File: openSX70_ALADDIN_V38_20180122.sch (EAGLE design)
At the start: 47 parts, among them Q1 5.8A/30V/35mΩ, Q2 5.8A/30V/35mΩ, U1 ATMEGA328P_TQFP, U3 BH1750FVI-TR, Y1 CSTCE16M0V53-R0

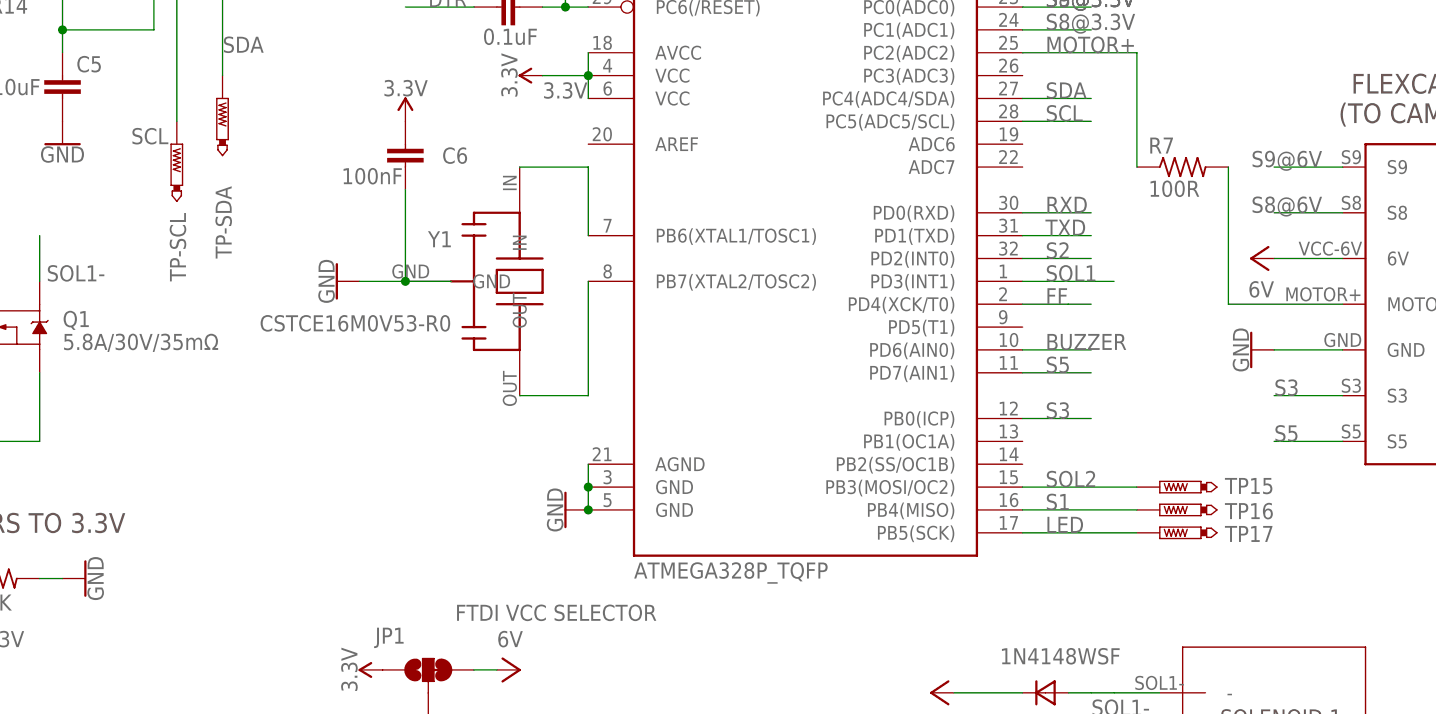
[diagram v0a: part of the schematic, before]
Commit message: "Saved" Aladdin regarding light-seal issue. Will manufacture. Current 2.8
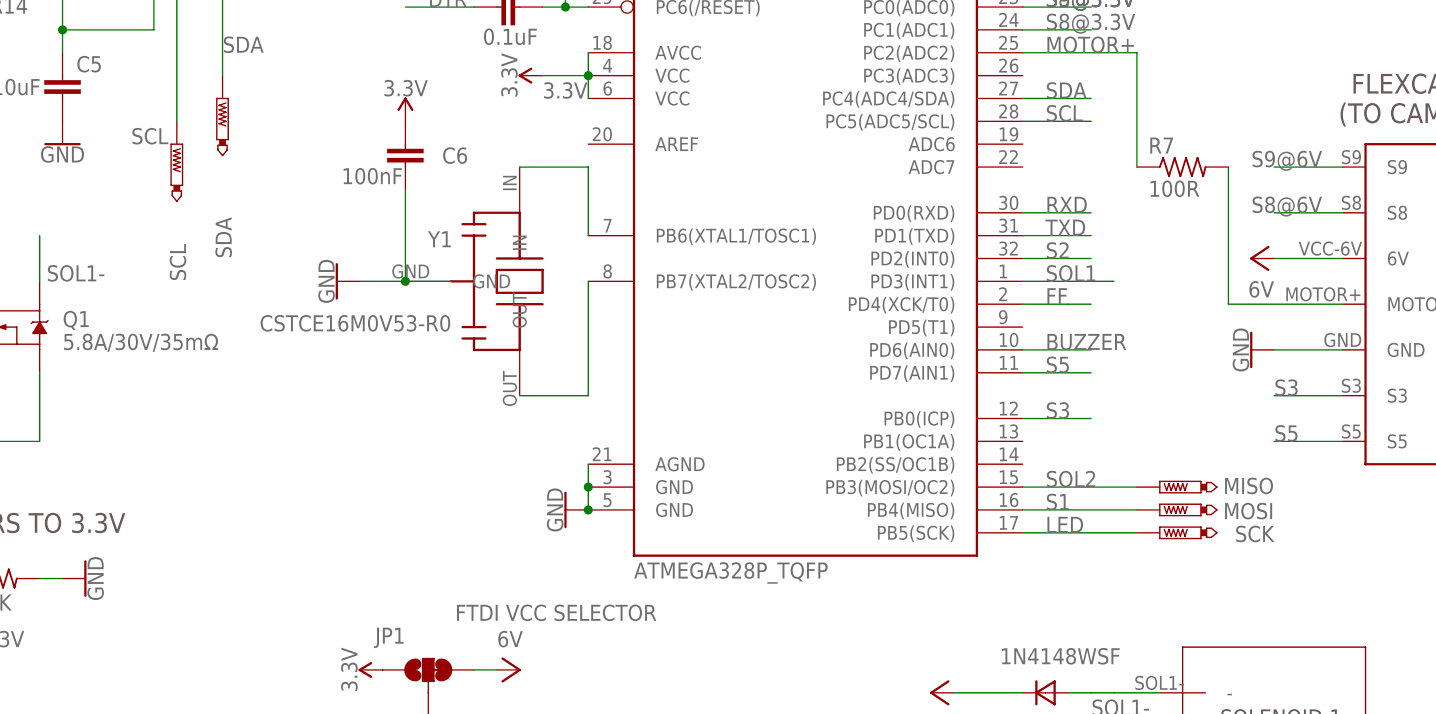
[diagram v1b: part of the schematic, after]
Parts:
- renumbered TP-SCL to SCL, TP-SDA to SDA, TP15 to MISO, TP16 to MOSI, TP17 to SCK
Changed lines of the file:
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@@
 <part name="P+9" library="openSX70" deviceset="VCC" device="" value="6V"/>
 <part name="GND4" library="SparkFun-PowerSymbols" library_urn="urn:adsk.eagle:library:530" deviceset="GND" device=""/>
-<part name="TP15" library="testpad" library_urn="urn:adsk.eagle:library:385" deviceset="PTR1" device="TP08R" package3d_urn="urn:adsk.eagle:package:27956/1" value="PTR1TP08R"/>
-<part name="TP16" library="testpad" library_urn="urn:adsk.eagle:library:385" deviceset="PTR1" device="TP08R" package3d_urn="urn:adsk.eagle:package:27956/1" value="PTR1TP08R"/>
-<part name="TP17" library="testpad" library_urn="urn:adsk.eagle:library:385" deviceset="PTR1" device="TP08R" package3d_urn="urn:adsk.eagle:package:27956/1" value="PTR1TP08R"/>
-<part name="TP-SDA" library="testpad" library_urn="urn:adsk.eagle:library:385" deviceset="PTR1" device="TP08R" package3d_urn="urn:adsk.eagle:package:27956/1" value="PTR1TP08R"/>
-<part name="TP-SCL" library="testpad" library_urn="urn:adsk.eagle:library:385" deviceset="PTR1" device="TP08R" package3d_urn="urn:adsk.eagle:package:27956/1" value="PTR1TP08R"/>
+<part name="MISO" library="testpad" library_urn="urn:adsk.eagle:library:385" deviceset="PTR1" device="TP08R" package3d_urn="urn:adsk.eagle:package:27956/1" value="PTR1TP08R"/>
+<part name="MOSI" library="testpad" library_urn="urn:adsk.eagle:library:385" deviceset="PTR1" device="TP08R" package3d_urn="urn:adsk.eagle:package:27956/1" value="PTR1TP08R"/>
+<part name="SCK" library="testpad" library_urn="urn:adsk.eagle:library:385" deviceset="PTR1" device="TP08R" package3d_urn="urn:adsk.eagle:package:27956/1" value="PTR1TP08R"/>
+<part name="SDA" library="testpad" library_urn="urn:adsk.eagle:library:385" deviceset="PTR1" device="TP08R" package3d_urn="urn:adsk.eagle:package:27956/1" value="PTR1TP08R"/>
+<part name="SCL" library="testpad" library_urn="urn:adsk.eagle:library:385" deviceset="PTR1" device="TP08R" package3d_urn="urn:adsk.eagle:package:27956/1" value="PTR1TP08R"/>
 </parts>
 <sheets>
@@
 <attribute name="VALUE" x="70.866" y="45.72" size="1.778" layer="96" rot="R270" align="top-center"/>
 </instance>
-<instance part="TP15" gate="G$1" x="208.28" y="73.66" smashed="yes" rot="R90">
+<instance part="MISO" gate="G$1" x="208.28" y="73.66" smashed="yes" rot="R90">
 <attribute name="NAME" x="220.98" y="74.676" size="1.778" layer="95" rot="R180"/>
 <attribute name="TP_SIGNAL_NAME" x="210.82" y="74.93" size="1.778" layer="97" rot="R90"/>
 </instance>
-<instance part="TP16" gate="G$1" x="208.28" y="71.12" smashed="yes" rot="R90">
+<instance part="MOSI" gate="G$1" x="208.28" y="71.12" smashed="yes" rot="R90">
 <attribute name="NAME" x="220.98" y="71.882" size="1.778" layer="95" rot="R180"/>
 <attribute name="TP_SIGNAL_NAME" x="210.82" y="72.39" size="1.778" layer="97" rot="R90"/>
 </instance>
-<instance part="TP17" gate="G$1" x="208.28" y="68.58" smashed="yes" rot="R90">
+<instance part="SCK" gate="G$1" x="208.28" y="68.58" smashed="yes" rot="R90">
 <attribute name="NAME" x="220.98" y="69.342" size="1.778" layer="95" rot="R180"/>
 <attribute name="TP_SIGNAL_NAME" x="210.82" y="69.85" size="1.778" layer="97" rot="R90"/>
 </instance>
-<instance part="TP-SDA" gate="G$1" x="104.14" y="116.84" smashed="yes">
+<instance part="SDA" gate="G$1" x="104.14" y="116.84" smashed="yes">
 <attribute name="NAME" x="105.156" y="99.06" size="1.778" layer="95" rot="R90"/>
 <attribute name="TP_SIGNAL_NAME" x="105.41" y="114.3" size="1.778" layer="97"/>
 </instance>
-<instance part="TP-SCL" gate="G$1" x="99.06" y="111.76" smashed="yes">
+<instance part="SCL" gate="G$1" x="99.06" y="111.76" smashed="yes">
 <attribute name="NAME" x="100.076" y="96.52" size="1.778" layer="95" rot="R90"/>
 <attribute name="TP_SIGNAL_NAME" x="100.33" y="109.22" size="1.778" layer="97"/>
@@
 <wire x1="193.04" y1="71.12" x2="205.74" y2="71.12" width="0.1524" layer="91"/>
 <label x="195.58" y="71.12" size="1.778" layer="95"/>
-<pinref part="TP16" gate="G$1" pin="TP"/>
+<pinref part="MOSI" gate="G$1" pin="TP"/>
 </segment>
 <segment>
@@
 <wire x1="193.04" y1="68.58" x2="205.74" y2="68.58" width="0.1524" layer="91"/>
 <label x="195.58" y="68.58" size="1.778" layer="95"/>
-<pinref part="TP17" gate="G$1" pin="TP"/>
+<pinref part="SCK" gate="G$1" pin="TP"/>
 </segment>
 <segment>
@@
 <wire x1="193.04" y1="73.66" x2="205.74" y2="73.66" width="0.1524" layer="91"/>
 <label x="195.58" y="73.66" size="1.778" layer="95"/>
-<pinref part="TP15" gate="G$1" pin="TP"/>
+<pinref part="MISO" gate="G$1" pin="TP"/>
 </segment>
 <segment>
@@
 <pinref part="U3" gate="G$1" pin="SDA"/>
 <label x="104.14" y="121.92" size="1.778" layer="95"/>
-<pinref part="TP-SDA" gate="G$1" pin="TP"/>
+<pinref part="SDA" gate="G$1" pin="TP"/>
 <wire x1="104.14" y1="119.38" x2="104.14" y2="129.54" width="0.1524" layer="91"/>
 </segment>
@@
 <wire x1="99.06" y1="129.54" x2="99.06" y2="114.3" width="0.1524" layer="91"/>
 <label x="93.98" y="111.76" size="1.778" layer="95"/>
-<pinref part="TP-SCL" gate="G$1" pin="TP"/>
-</segment>
-</net>
+<pinref part="SCL" gate="G$1" pin="TP"/>
+</segment>
+</net>

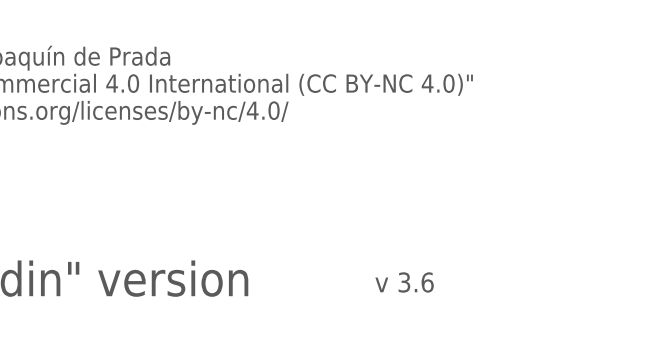
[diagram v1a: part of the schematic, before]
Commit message: Fixing little things in all Aladdin boards
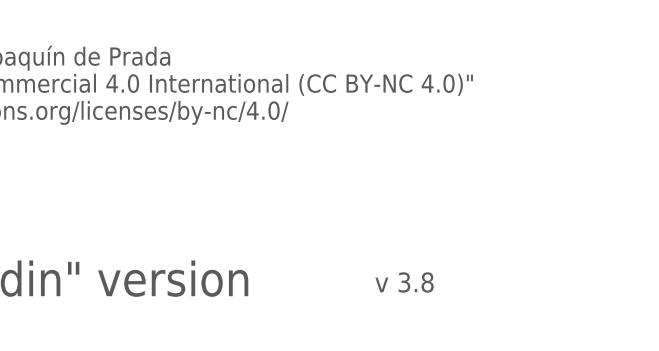
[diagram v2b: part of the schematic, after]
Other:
- note added: "v 3.8"
- note removed: "v 3.6"
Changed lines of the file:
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@@
 or
 FLASH</text>
-<text x="246.38" y="2.54" size="2.1844" layer="97" align="center">v 3.6</text>
+<text x="246.38" y="2.54" size="2.1844" layer="97" align="center">v 3.8</text>
 <text x="203.454" y="24.638" size="2.0066" layer="97" align="center">Design by Joaquín de Prada
 Creative Commons "Attribution-NonCommercial 4.0 International (CC BY-NC 4.0)"

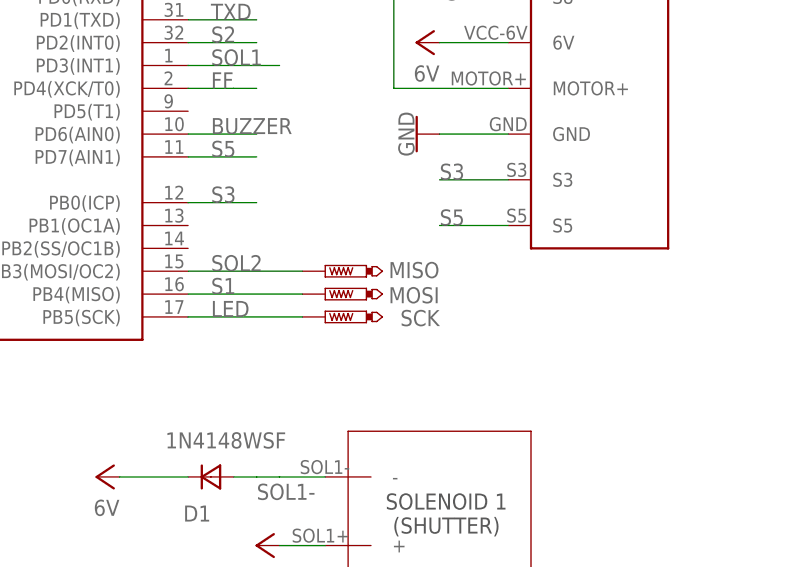
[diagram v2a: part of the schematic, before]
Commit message: Changed MISO/MOSI was all wrong
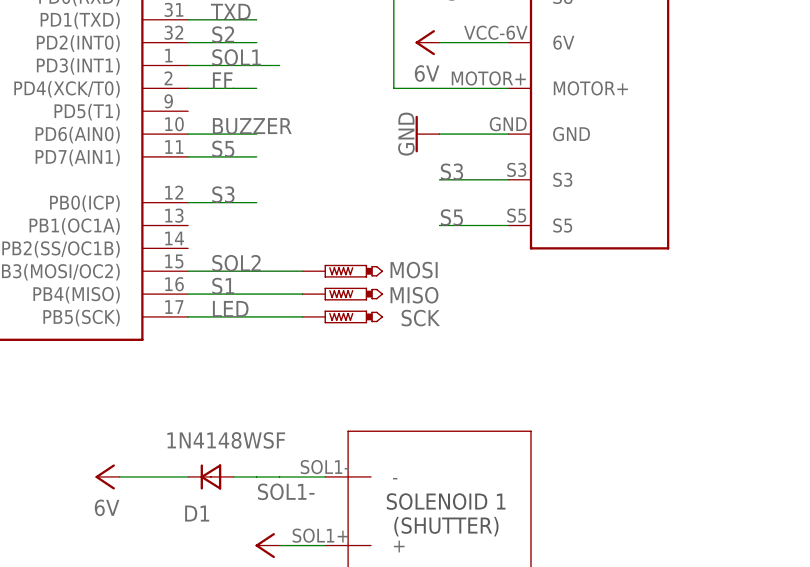
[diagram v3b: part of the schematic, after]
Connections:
- net S1: now also MISO.TP; no longer MOSI.TP
- net SOL2: now also MOSI.TP; no longer MISO.TP
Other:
- moved on the sheet: MISO, MOSI
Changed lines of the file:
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@@
 <part name="P+9" library="openSX70" deviceset="VCC" device="" value="6V"/>
 <part name="GND4" library="SparkFun-PowerSymbols" library_urn="urn:adsk.eagle:library:530" deviceset="GND" device=""/>
+<part name="MOSI" library="testpad" library_urn="urn:adsk.eagle:library:385" deviceset="PTR1" device="TP08R" package3d_urn="urn:adsk.eagle:package:27956/1" value="PTR1TP08R"/>
 <part name="MISO" library="testpad" library_urn="urn:adsk.eagle:library:385" deviceset="PTR1" device="TP08R" package3d_urn="urn:adsk.eagle:package:27956/1" value="PTR1TP08R"/>
-<part name="MOSI" library="testpad" library_urn="urn:adsk.eagle:library:385" deviceset="PTR1" device="TP08R" package3d_urn="urn:adsk.eagle:package:27956/1" value="PTR1TP08R"/>
 <part name="SCK" library="testpad" library_urn="urn:adsk.eagle:library:385" deviceset="PTR1" device="TP08R" package3d_urn="urn:adsk.eagle:package:27956/1" value="PTR1TP08R"/>
 <part name="SDA" library="testpad" library_urn="urn:adsk.eagle:library:385" deviceset="PTR1" device="TP08R" package3d_urn="urn:adsk.eagle:package:27956/1" value="PTR1TP08R"/>
@@
 <attribute name="VALUE" x="70.866" y="45.72" size="1.778" layer="96" rot="R270" align="top-center"/>
 </instance>
-<instance part="MISO" gate="G$1" x="208.28" y="73.66" smashed="yes" rot="R90">
+<instance part="MOSI" gate="G$1" x="208.28" y="73.66" smashed="yes" rot="R90">
 <attribute name="NAME" x="220.98" y="74.676" size="1.778" layer="95" rot="R180"/>
 <attribute name="TP_SIGNAL_NAME" x="210.82" y="74.93" size="1.778" layer="97" rot="R90"/>
 </instance>
-<instance part="MOSI" gate="G$1" x="208.28" y="71.12" smashed="yes" rot="R90">
+<instance part="MISO" gate="G$1" x="208.28" y="71.12" smashed="yes" rot="R90">
 <attribute name="NAME" x="220.98" y="71.882" size="1.778" layer="95" rot="R180"/>
 <attribute name="TP_SIGNAL_NAME" x="210.82" y="72.39" size="1.778" layer="97" rot="R90"/>
@@
 <wire x1="193.04" y1="71.12" x2="205.74" y2="71.12" width="0.1524" layer="91"/>
 <label x="195.58" y="71.12" size="1.778" layer="95"/>
-<pinref part="MOSI" gate="G$1" pin="TP"/>
+<pinref part="MISO" gate="G$1" pin="TP"/>
 </segment>
 <segment>
@@
 <wire x1="193.04" y1="73.66" x2="205.74" y2="73.66" width="0.1524" layer="91"/>
 <label x="195.58" y="73.66" size="1.778" layer="95"/>
-<pinref part="MISO" gate="G$1" pin="TP"/>
-</segment>
-<segment>
+<pinref part="MOSI" gate="G$1" pin="TP"/>
+</segment>
+<segment>
